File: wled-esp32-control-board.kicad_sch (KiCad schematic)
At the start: 32 parts, among them J101 Conn_01x03, J102 Conn_01x03, J103 Conn_01x03, J104 Conn_01x03, J3 Conn_02x03_Odd_Even, SW101 SW_SPDT, SW103 SW_Push, SW105 SW_Push, U102 74AHCT1G125, U103 ESP32-WROOM-32, U106 TSOP382xx

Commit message: add mouser part numbers
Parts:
- C101: Mouser (none) -> 581-06036D226MAT2A
- C102, C104: Mouser (none) -> 581-06035C104KAT2A
- LED1: Mouser (none) -> 710-150060BS75000
- LED2: Mouser (none) -> 710-150060VS75000
- LED3: Mouser (none) -> 710-150060RS75000
- R10, R14, R9: Mouser (none) -> 603-RC0603FR-072KL
- R101: Mouser (none) -> 603-RC0603FR-0710KL
- R102, R103, R106, R108: Mouser (none) -> 603-RT0603FRE10100RL
- SW103, SW105: Mouser (none) -> 179-TS18525SL160SMTT
- U102: Mouser (none) -> 595-SNAHCT1G125DBVR
- U103: Mouser (none) -> 356-ESP32WRM32E132PH
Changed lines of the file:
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@@
+      (effects (font (size 1.27 1.27)) hide)
+    )
+    (property "Mouser" "595-SNAHCT1G125DBVR" (at 224.79 99.06 0)
       (effects (font (size 1.27 1.27)) hide)
     )
@@
     )
     (property "LCSC" "C22775" (at 240.03 99.06 0)
+      (effects (font (size 1.27 1.27)) hide)
+    )
+    (property "Mouser" "603-RT0603FRE10100RL" (at 240.03 99.06 0)
       (effects (font (size 1.27 1.27)) hide)
     )
@@
       (effects (font (size 1.27 1.27)) hide)
     )
+    (property "Mouser" "595-SNAHCT1G125DBVR" (at 224.79 68.58 0)
+      (effects (font (size 1.27 1.27)) hide)
+    )
     (pin "1")
     (pin "2")
@@
       (effects (font (size 1.27 1.27)) hide)
     )
+    (property "Mouser" "603-RC0603FR-072KL" (at 64.77 91.44 0)
+      (effects (font (size 1.27 1.27)) hide)
+    )
     (pin "1")
     (pin "2")
@@
     )
     (property "LCSC" "C22975" (at 64.77 82.55 0)
+      (effects (font (size 1.27 1.27)) hide)
+    )
+    (property "Mouser" "603-RC0603FR-072KL" (at 64.77 82.55 0)
       (effects (font (size 1.27 1.27)) hide)
     )
@@
       (effects (font (size 1.27 1.27)) hide)
     )
+    (property "Mouser" "710-150060RS75000" (at 72.39 100.33 0)
+      (effects (font (size 1.27 1.27)) hide)
+    )
     (pin "1")
     (pin "2")
@@
     )
     (property "LCSC" "C22775" (at 240.03 68.58 0)
+      (effects (font (size 1.27 1.27)) hide)
+    )
+    (property "Mouser" "603-RT0603FRE10100RL" (at 240.03 68.58 0)
       (effects (font (size 1.27 1.27)) hide)
     )
@@
       (effects (font (size 1.27 1.27)) hide)
     )
+    (property "Mouser" "595-SNAHCT1G125DBVR" (at 224.79 129.54 0)
+      (effects (font (size 1.27 1.27)) hide)
+    )
     (pin "1")
     (pin "2")
@@
     )
     (property "LCSC" "C701341" (at 140.97 73.66 0)
+      (effects (font (size 1.27 1.27)) hide)
+    )
+    (property "Mouser" "356-ESP32WRM32E132PH" (at 140.97 73.66 0)
       (effects (font (size 1.27 1.27)) hide)
     )
@@
       (effects (font (size 1.27 1.27)) hide)
     )
+    (property "Mouser" "710-150060VS75000" (at 72.39 91.44 0)
+      (effects (font (size 1.27 1.27)) hide)
+    )
     (pin "1")
     (pin "2")
@@
       (effects (font (size 1.27 1.27)) hide)
     )
+    (property "Mouser" "603-RC0603FR-072KL" (at 64.77 100.33 0)
+      (effects (font (size 1.27 1.27)) hide)
+    )
     (pin "1")
     (pin "2")
@@
       (effects (font (size 1.27 1.27)) hide)
     )
+    (property "Mouser" "581-06036D226MAT2A" (at 119.38 30.48 0)
+      (effects (font (size 1.27 1.27)) hide)
+    )
     (pin "1")
     (pin "2")
@@
       (effects (font (size 1.27 1.27)) hide)
     )
+    (property "Mouser" "603-RT0603FRE10100RL" (at 240.03 129.54 0)
+      (effects (font (size 1.27 1.27)) hide)
+    )
     (pin "1")
     (pin "2")
@@
       (effects (font (size 1.27 1.27)) hide)
     )
+    (property "Mouser" "603-RT0603FRE10100RL" (at 240.03 38.1 0)
+      (effects (font (size 1.27 1.27)) hide)
+    )
     (pin "1")
     (pin "2")
@@
     )
     (property "LCSC" "C318884" (at 34.29 99.06 0)
+      (effects (font (size 1.27 1.27)) hide)
+    )
+    (property "Mouser" "179-TS18525SL160SMTT" (at 34.29 99.06 0)
       (effects (font (size 1.27 1.27)) hide)
     )
@@
       (effects (font (size 1.27 1.27)) hide)
     )
+    (property "Mouser" "603-RC0603FR-0710KL" (at 107.95 35.56 0)
+      (effects (font (size 1.27 1.27)) hide)
+    )
     (pin "1")
     (pin "2")
@@
     )
     (property "LCSC" "C318884" (at 34.29 80.01 0)
+      (effects (font (size 1.27 1.27)) hide)
+    )
+    (property "Mouser" "179-TS18525SL160SMTT" (at 34.29 80.01 0)
       (effects (font (size 1.27 1.27)) hide)
     )
@@
       (effects (font (size 1.27 1.27)) hide)
     )
+    (property "Mouser" "595-SNAHCT1G125DBVR" (at 224.79 38.1 0)
+      (effects (font (size 1.27 1.27)) hide)
+    )
     (pin "1")
     (pin "2")
@@
       (effects (font (size 1.27 1.27)) hide)
     )
+    (property "Mouser" "710-150060BS75000" (at 72.39 82.55 0)
+      (effects (font (size 1.27 1.27)) hide)
+    )
     (pin "1")
     (pin "2")
@@
     )
     (property "LCSC" "C14663" (at 129.54 30.48 0)
+      (effects (font (size 1.27 1.27)) hide)
+    )
+    (property "Mouser" "581-06035C104KAT2A" (at 129.54 30.48 0)
       (effects (font (size 1.27 1.27)) hide)
     )
@@
       (effects (font (size 1.27 1.27)) hide)
     )
+    (property "Mouser" "581-06035C104KAT2A" (at 107.95 48.26 0)
+      (effects (font (size 1.27 1.27)) hide)
+    )

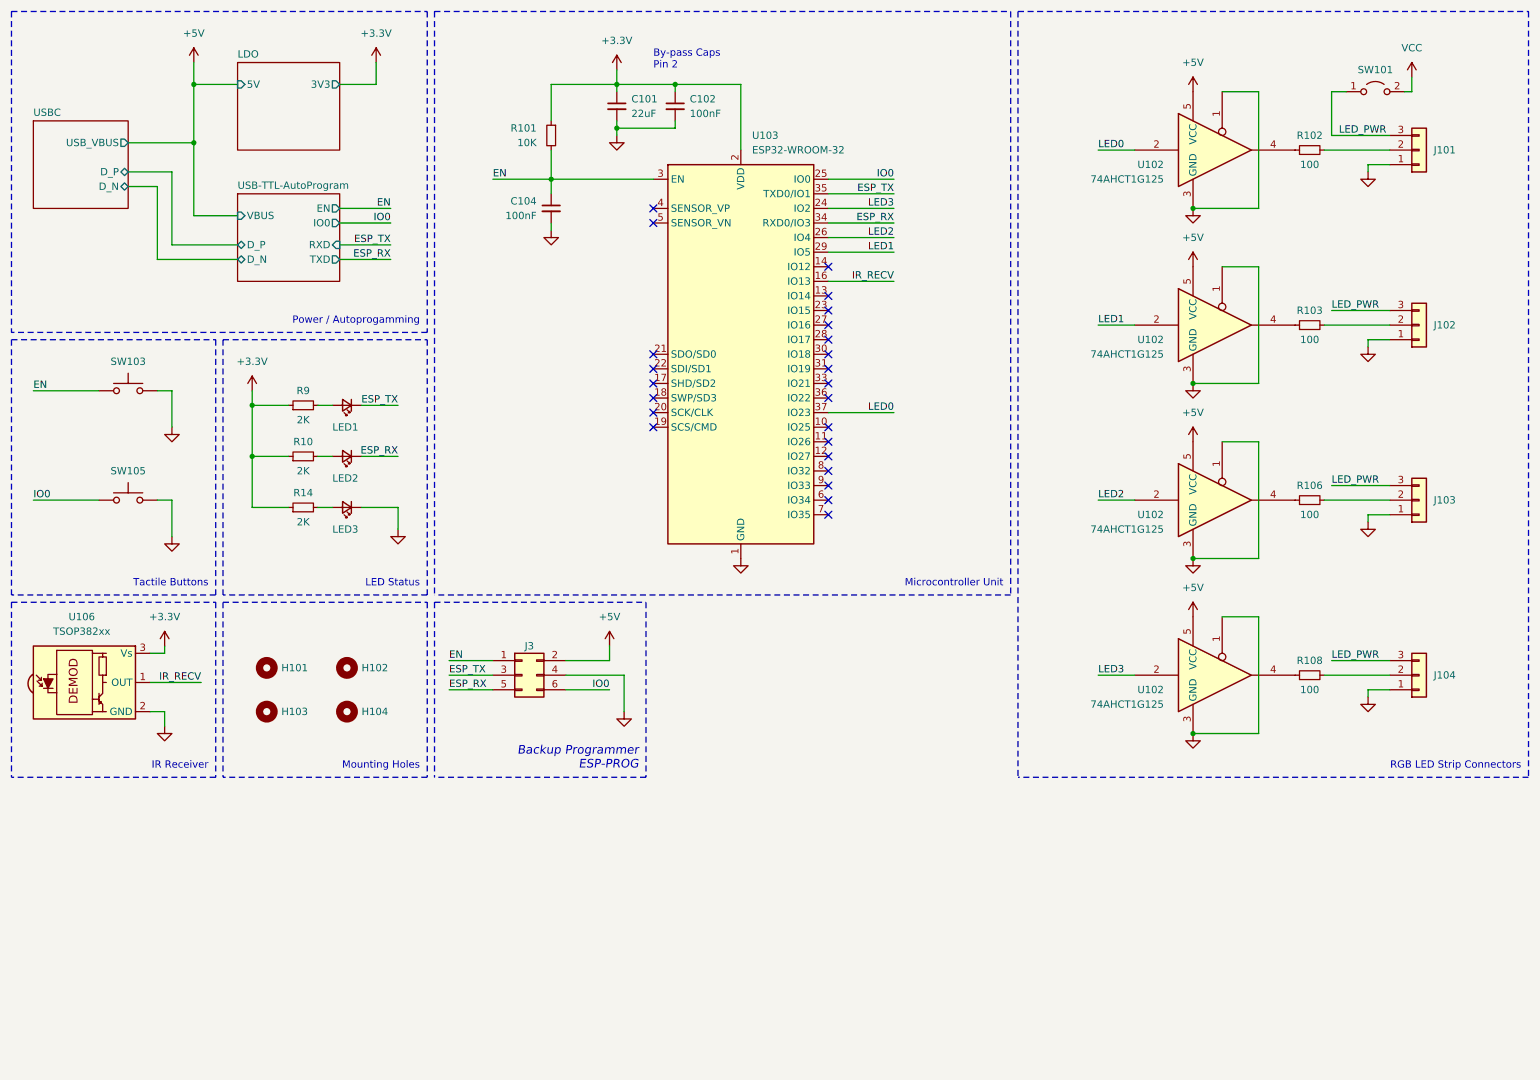
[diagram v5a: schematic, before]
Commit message: update design to replace CP2102 and LDO
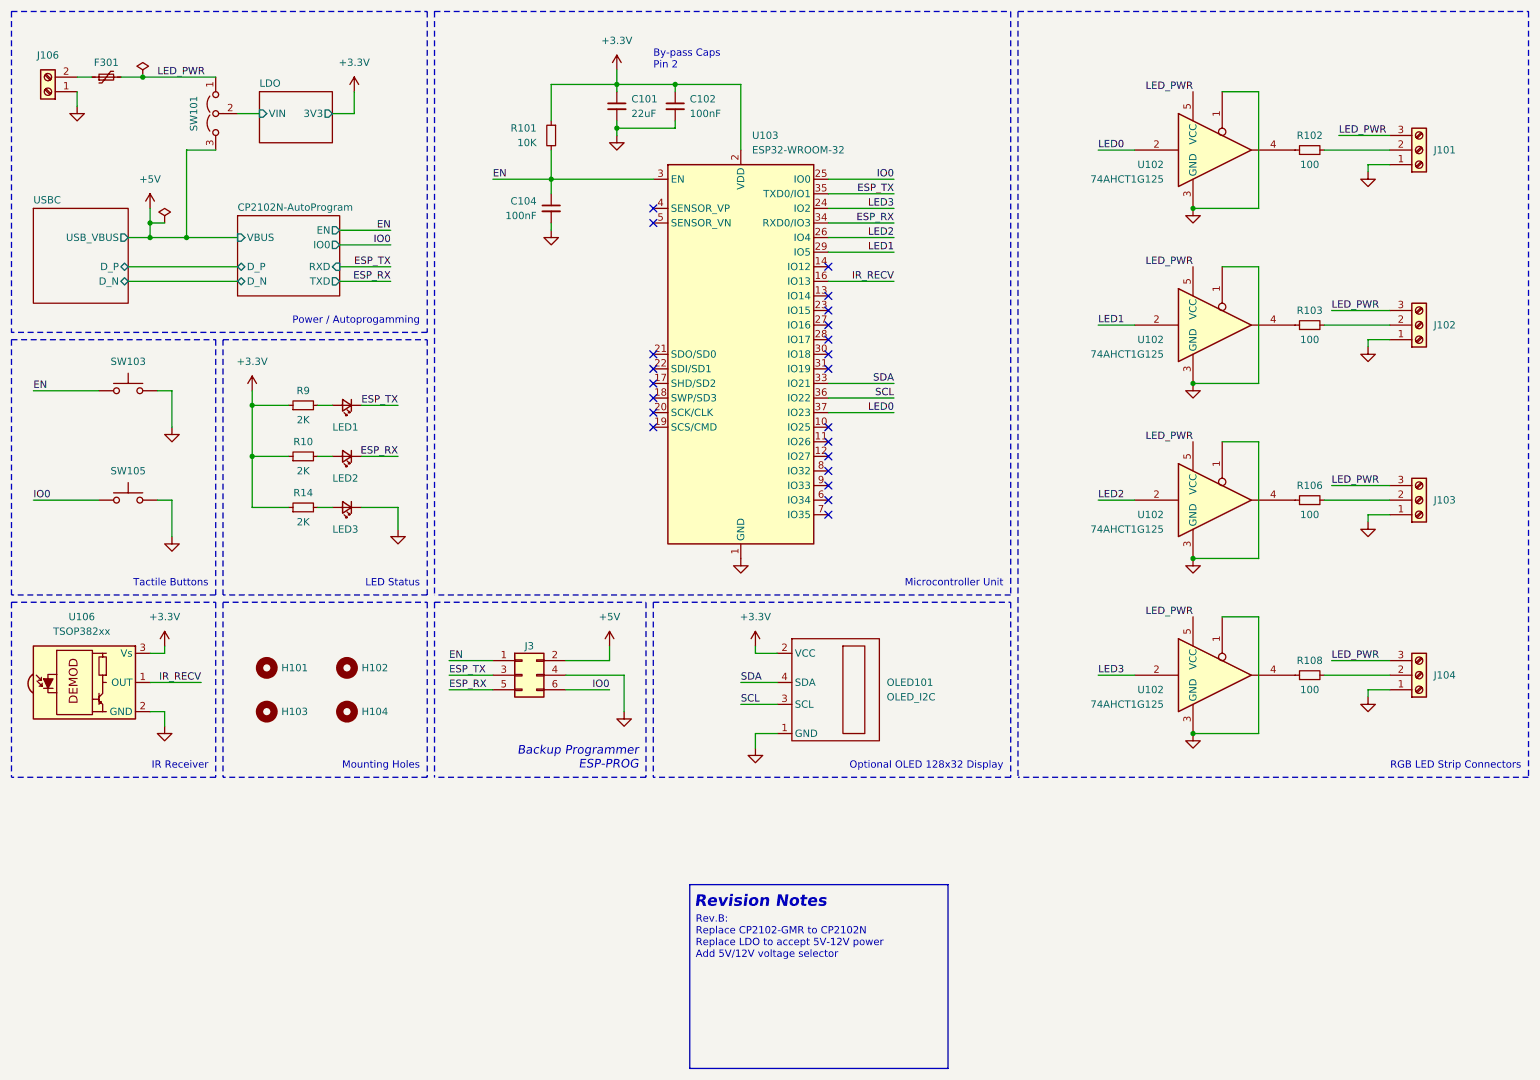
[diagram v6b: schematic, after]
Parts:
- added F301: Polyfuse_Small, Fuse:Fuse_2920_7451Metric, symbol Device:Polyfuse_Small
- added J106: Screw_Terminal_01x02, User_Footprint:397730002, symbol Connector:Screw_Terminal_01x02
- added OLED101: OLED_I2C, User_Footprint:OLED_128x32_I2C_4pins, symbol User Symbols:OLED_I2C
- J101, J102, J103, J104: symbol Connector_Generic:Conn_01x03 -> Connector:Screw_Terminal_01x03; now in the parts list
- SW101: footprint Connector_PinHeader_2.54mm:PinHeader_1x02_P2.54mm_Vertical -> Connector_PinHeader_2.54mm:PinHeader_1x03_P2.54mm_Vertical; symbol Jumper:Jumper_2_Open -> Jumper:Jumper_3_Open; now in the parts list
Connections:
- net +3.3V: now also OLED101.2 (VCC)
- net +5V: now also SW101.3 (B); no longer U102.5 (VCC), U102.5 (VCC), U102.5 (VCC), U102.5 (VCC)
- net GND: now also J106.1 (Pin_1), OLED101.1 (GND)
- net LED_PWR: now also U102.5 (VCC), U102.5 (VCC), U102.5 (VCC), U102.5 (VCC), F301.2
- net SDA: now reaches U103.33 (IO21)
- net SDA: now also OLED101.4 (SDA)
- net SCL: now reaches U103.36 (IO22)
- net SCL: now also OLED101.3 (SCL)
- net VCC renamed LDO/VIN
- new net: F301.1, J106.2 (Pin_2)
- no-connect marks 24 -> 22
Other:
- removed sheet USB-TTL-AutoProgram
- added sheet CP2102N-AutoProgram (usb_uart_serial.kicad_sch)
- sheet LDO ports: added VIN; removed 5V
- note added: "Optional OLED 128x32 Display"
- note added: "Revision Notes"

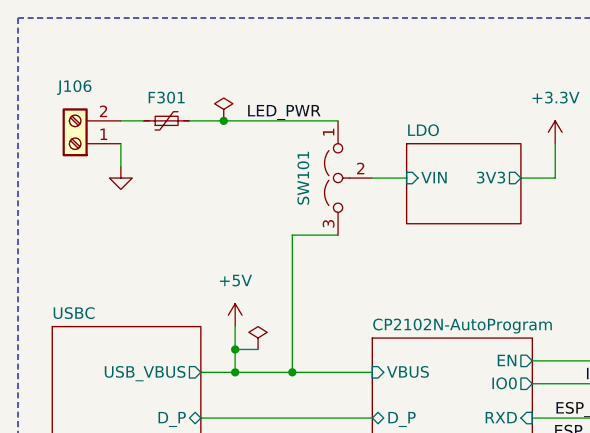
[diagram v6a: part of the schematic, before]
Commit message: refactor to accept 12V power
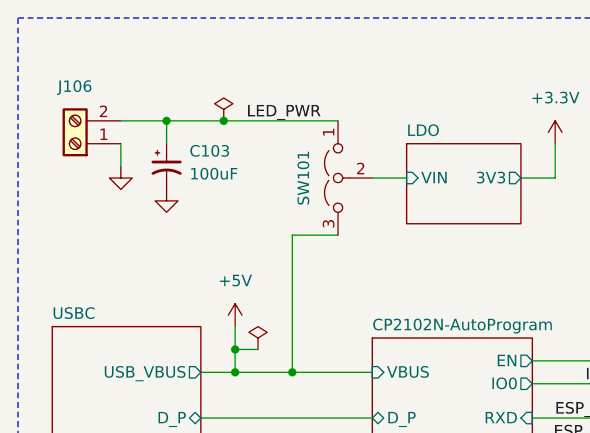
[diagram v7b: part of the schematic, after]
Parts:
- removed F301: Polyfuse_Small, Fuse:Fuse_2920_7451Metric, symbol Device:Polyfuse_Small
- added C103: 100uF, Capacitor_THT:CP_Radial_D5.0mm_P2.00mm, symbol Device:C_Polarized_Small_US
- U103: footprint User_Footprint:ESP32-WROOM-32 -> User_Footprint:ESP32­-WROOM­-32E
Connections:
- net GND: now also C103.2
- net LED_PWR: now also J106.2 (Pin_2), C103.1
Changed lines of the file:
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@@
   (junction (at 38.1 50.8) (diameter 0) (color 0 0 0 0)
+  )
+  (junction (at 30.48 25.4) (diameter 0) (color 0 0 0 0)
   )
   (junction (at 119.38 26.67) (diameter 0) (color 0 0 0 0)
@@
     (stroke (width 0) (type default))
   )
-  (wire (pts (xy 33.02 25.4) (xy 36.83 25.4))
-    (stroke (width 0) (type default))
-  )
   (wire (pts (xy 203.2 68.58) (xy 209.55 68.58))
     (stroke (width 0) (type default))
@@
     (stroke (width 0) (type default))
   )
+  (wire (pts (xy 30.48 25.4) (xy 36.83 25.4))
+    (stroke (width 0) (type default))
+  )
   (wire (pts (xy 107.95 26.67) (xy 107.95 33.02))
     (stroke (width 0) (type default))
   )
-  (wire (pts (xy 25.4 25.4) (xy 27.94 25.4))
+  (wire (pts (xy 25.4 25.4) (xy 30.48 25.4))
     (stroke (width 0) (type default))
   )
@@
   )
   (wire (pts (xy 34.29 53.34) (xy 38.1 53.34))
+    (stroke (width 0) (type default))
+  )
+  (wire (pts (xy 30.48 27.94) (xy 30.48 25.4))
     (stroke (width 0) (type default))
   )
@@
     )
   )
-  (symbol (lib_id "Device:Polyfuse_Small") (at 30.48 25.4 90) (unit 1)
-    (in_bom yes) (on_board yes) (dnp no)
-    (property "Reference" "F301" (at 30.48 22.86 90)
-      (effects (font (size 1.27 1.27)))
-    )
-    (property "Value" "Polyfuse_Small" (at 30.48 21.59 90)
-      (effects (font (size 1.27 1.27)) hide)
-    )
-    (property "Footprint" "Fuse:Fuse_2920_7451Metric" (at 35.56 24.13 0)
-      (effects (font (size 1.27 1.27)) (justify left) hide)
-    )
-    (property "Datasheet" "~" (at 30.48 25.4 0)
-      (effects (font (size 1.27 1.27)) hide)
-    )
-    (property "LCSC" "C207086" (at 30.48 25.4 0)
-      (effects (font (size 1.27 1.27)) hide)
-    )
-    (property "Mouser" "576-2920L185" (at 30.48 25.4 0)
-      (effects (font (size 1.27 1.27)) hide)
-    )
-    (pin "2")
-    (pin "1")
-    (instances
-      (project "wled-esp32-control-board"
-        (path "/39949f26-7b4e-4f4c-975a-4ef261468b2a/d1f69b69-3231-4944-97e3-fdd35c90f911"
-          (reference "F301") (unit 1)
-        )
-        (path "/39949f26-7b4e-4f4c-975a-4ef261468b2a"
-          (reference "F101") (unit 1)
-        )
-      )
-    )
-  )
   (symbol (lib_id "power:+3.3V") (at 143.51 124.46 0) (unit 1)
     (in_bom yes) (on_board yes) (dnp no) (fields_autoplaced)
@@
       (effects (font (size 1.27 1.27)) (justify left))
     )
-    (property "Footprint" "User_Footprint:ESP32-WROOM-32" (at 140.97 111.76 0)
+    (property "Footprint" "User_Footprint:ESP32­-WROOM­-32E" (at 140.97 111.76 0)
       (effects (font (size 1.27 1.27)) hide)
     )
@@
     )
   )
+  (symbol (lib_id "power:GND") (at 30.48 33.02 0) (unit 1)
+    (in_bom yes) (on_board yes) (dnp no) (fields_autoplaced)
+    (property "Reference" "#PWR0111" (at 30.48 39.37 0)
+      (effects (font (size 1.27 1.27)) hide)
+    )
+    (property "Value" "GND" (at 30.48 38.1 0)
+      (effects (font (size 1.27 1.27)) hide)
+    )
+    (property "Footprint" "" (at 30.48 33.02 0)
+      (effects (font (size 1.27 1.27)) hide)
+    )
+    (property "Datasheet" "" (at 30.48 33.02 0)
+      (effects (font (size 1.27 1.27)) hide)
+    )
+    (pin "1")
+    (instances
+      (project "wled-esp32-control-board"
+        (path "/39949f26-7b4e-4f4c-975a-4ef261468b2a"
+          (reference "#PWR0111") (unit 1)
+        )
+      )
+    )
+  )
   (symbol (lib_id "Device:LED_Small") (at 72.39 91.44 180) (unit 1)
     (in_bom yes) (on_board yes) (dnp no)
@@
         )
       )
+    )
+  )
+  (symbol (lib_id "Device:C_Polarized_Small_US") (at 30.48 30.48 0) (unit 1)
+    (in_bom yes) (on_board yes) (dnp no) (fields_autoplaced)
+    (property "Reference" "C103" (at 33.02 28.7782 0)
+      (effects (font (size 1.27 1.27)) (justify left))
+    )
+    (property "Value" "100uF" (at 33.02 31.3182 0)
+      (effects (font (size 1.27 1.27)) (justify left))
+    )
+    (property "Footprint" "Capacitor_THT:CP_Radial_D5.0mm_P2.00mm" (at 30.48 30.48 0)
+      (effects (font (size 1.27 1.27)) hide)
+    )
+    (property "Datasheet" "~" (at 30.48 30.48 0)
+      (effects (font (size 1.27 1.27)) hide)
+    )
+    (property "LCSC" "" (at 30.48 30.48 0)
+      (effects (font (size 1.27 1.27)) hide)
+    )
+    (property "Mouser" "232-25YXJ100M5X11" (at 30.48 30.48 0)
+      (effects (font (size 1.27 1.27)) hide)
+    )
+    (pin "2")
+    (pin "1")
+    (instances
+      (project "wled-esp32-control-board"
+        (path "/39949f26-7b4e-4f4c-975a-4ef261468b2a"
+          (reference "C103") (unit 1)
+        )
+      )
